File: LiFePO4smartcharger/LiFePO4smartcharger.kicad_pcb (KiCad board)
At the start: 2 copper layers, 99.3 x 98.6 mm, 106 parts, among them J1 Conn_01x02, J10 Conn_01x01, J11 Conn_01x01, J12 Conn_01x04, J13 Conn_01x01, J14 Conn_01x02, J2 Conn_02x03_Odd_Even, J3 Conn_01x02, J4 Conn_01x02, J5 Conn_01x02, J6 Conn_01x01, J7 Conn_01x01, J8 Conn_01x02, J9 Conn_01x02, Q1 TIP42, Q2 TIP41, Q3 2N3906, Q4 TIP41C, T1 Transformer_1P1Sdotted, U1 ATMEGA328P-PU, U2 LM358, U3 LCD-016N002L, U4 TL494, U9 LM7805_TO220, X3 16MHz

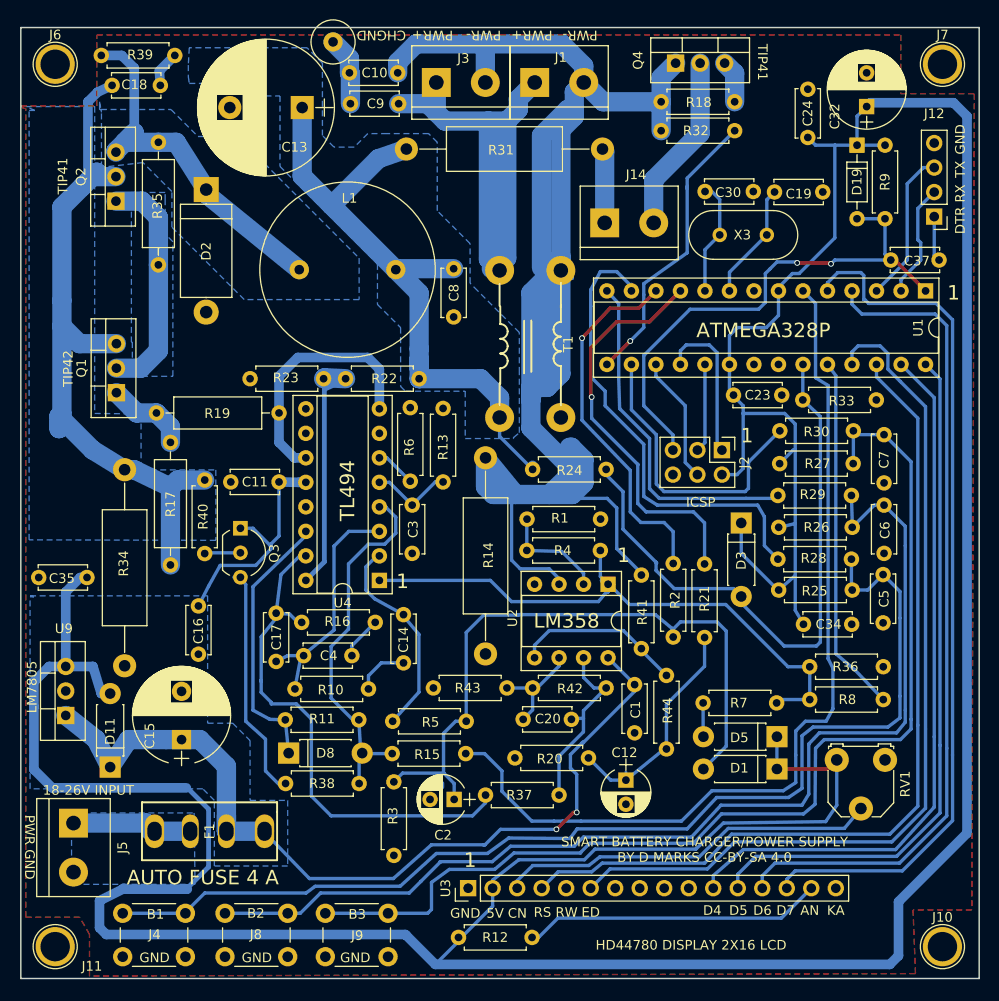
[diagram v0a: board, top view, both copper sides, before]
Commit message: Fixes to allow for larger components
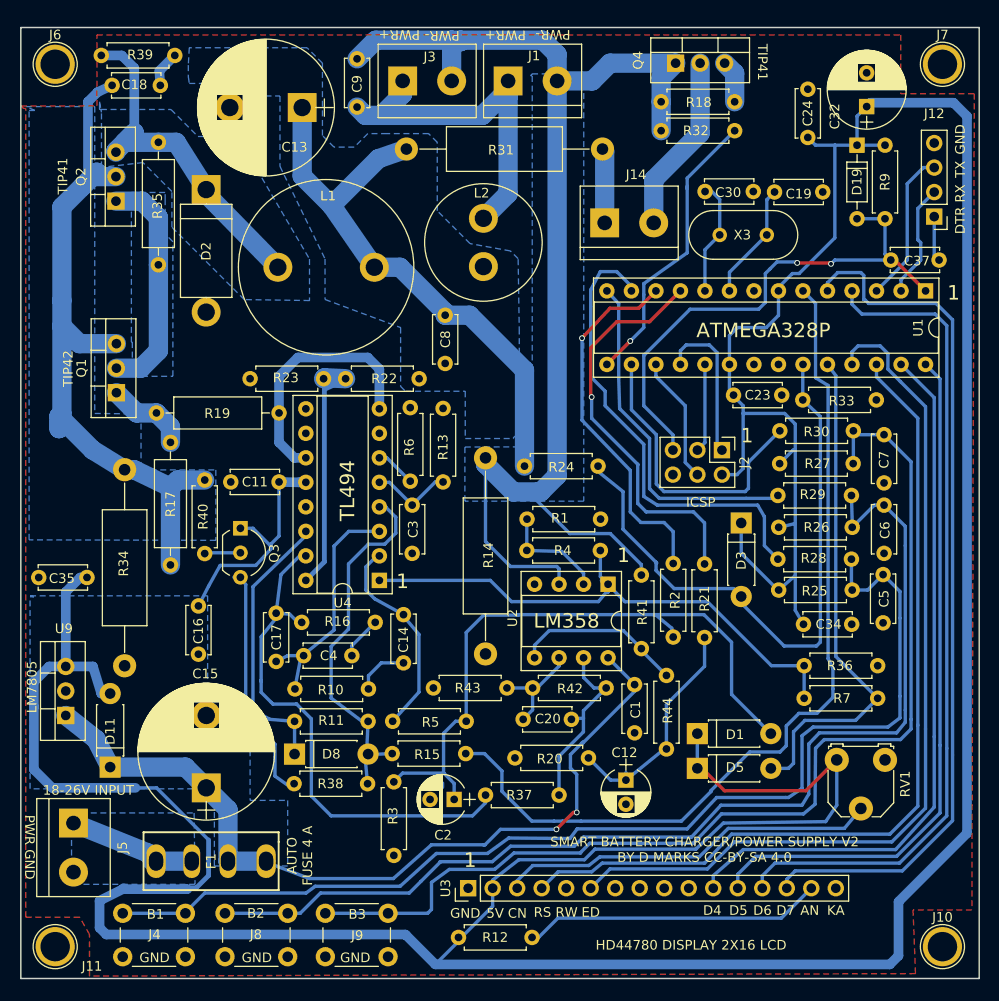
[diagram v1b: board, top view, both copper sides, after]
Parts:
- removed C10: 100nF, Capacitors_THT:C_Disc_D5.0mm_W2.5mm_P5.00mm
- removed J13: Conn_01x01, Connectors:1pin
- removed R8: 10k, Resistors_THT:R_Axial_DIN0207_L6.3mm_D2.5mm_P7.62mm_Horizontal
- removed T1: Transformer_1P1Sdotted, LiFePO4smartcharger:GenericCMCL3
- added L2: 10 uH, Inductors_THT:L_Radial_D12.0mm_P5.00mm_Fastron_11P, F.Cu at (90.2, 55.0)
- C15: footprint Capacitors_THT:CP_Radial_D10.0mm_P5.00mm -> Capacitors_THT:CP_Radial_D14.0mm_P7.50mm
- moved R7 18.1 mm to (131.0, 99.7), turned to 180 degrees
- moved D1 9.03 mm to (112.3, 103.4), turned to 0 degrees
- moved D5 8.88 mm to (112.3, 107.0), turned to 0 degrees
- moved C15 5.62 mm to (61.5, 109.0)
- moved C8 4.90 mm to (86.2, 60.0)
- moved C9 4.32 mm to (77.1, 38.5), turned to 90 degrees
- moved J3 3.49 mm to (81.8, 35.7)
- moved F1 3.10 mm to (62.0, 116.6)
- moved J1 2.76 mm to (92.7, 35.7)
- moved L1 2.23 mm to (68.9, 55.0)
- moved R11 0.97 mm to (70.6, 102.1)
- moved R24 0.91 mm to (102.1, 75.7)
- moved R38 0.88 mm to (78.2, 108.6)
- moved D8 0.62 mm to (70.6, 105.5)
- moved R36 0.59 mm to (123.4, 96.3)
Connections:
- C9 pad 2: Net-(C10-Pad1) -> CURRENTSHUNT
- D5 pad 2: Net-(D5-Pad2) -> A1
- R7 pad 1: Net-(D5-Pad2) -> A1
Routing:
- net CURRENTSHUNT: track 191.0 -> 139.8 mm
- net A1: track 38.0 -> 53.5 mm
- net Net-(C9-Pad1): track 52.9 -> 37.6 mm
- net Net-(C13-Pad1): track 69.5 -> 59.9 mm
- net +5V: track 421.4 -> 430.8 mm
- net Net-(C10-Pad1): track 7.15 -> 0.00 mm
- net +24V: track 117.4 -> 111.8 mm
- net Net-(R36-Pad1): track 65.7 -> 61.0 mm
- net Net-(D5-Pad2): track 3.51 -> 0.00 mm
- net SHUTDOWN: track 95.0 -> 92.3 mm
- net Net-(C2-Pad1): track 70.8 -> 68.9 mm
- net Net-(D2-Pad1): track 40.9 -> 39.1 mm
- net Net-(D8-Pad1): track 27.9 -> 28.8 mm
- net A0: track 63.6 -> 64.5 mm
- net Net-(F1-Pad2): track 12.5 -> 13.2 mm
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- added copper zone on B.Cu, net CURRENTSHUNT
- removed copper zone on B.Cu, net Net-(C9-Pad1)
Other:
- board text added: "SMART BATTERY CHARGER/POWER SUPPLY V2 BY D MARKS CC-BY-SA 4.0"
- board text removed: "CHGND"
- board text removed: "SMART BATTERY CHARGER/POWER SUPPLY BY D MARKS CC-BY-SA 4.0"

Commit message: Before switching VOLTAGESET CURRENTSET pins
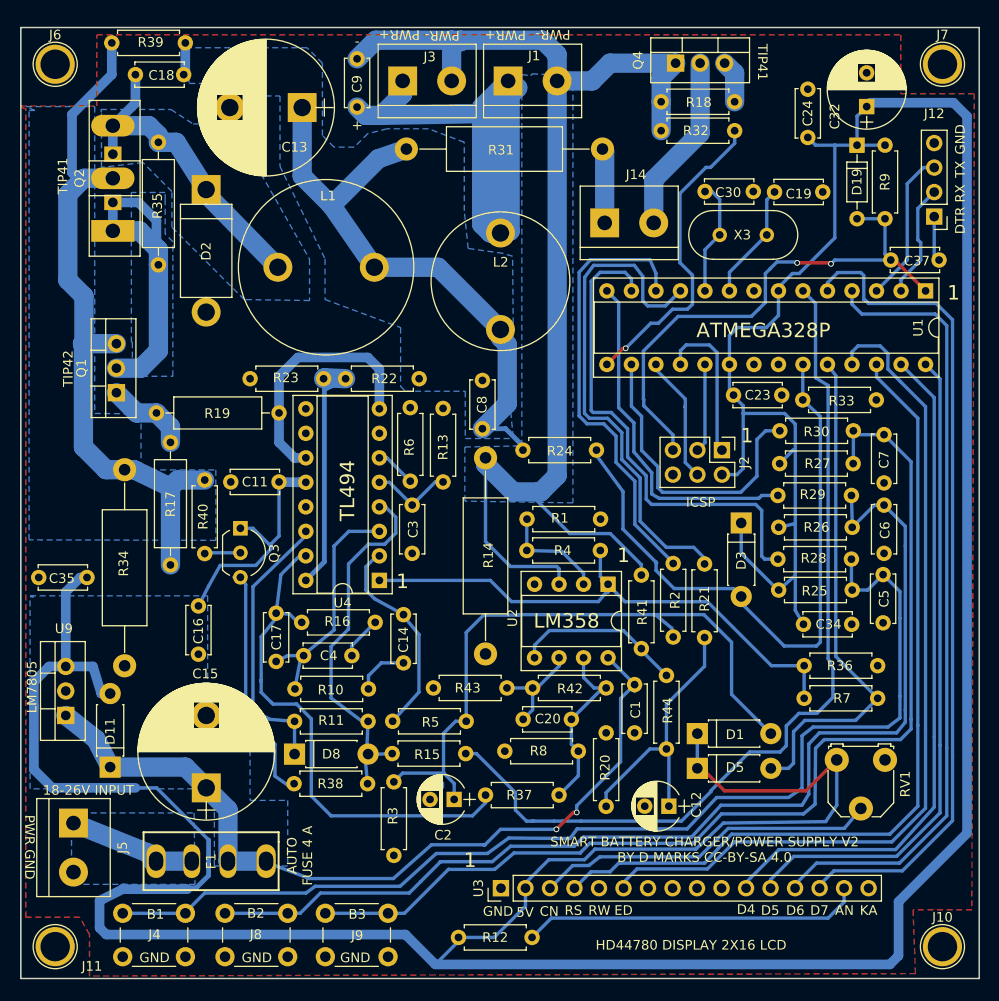
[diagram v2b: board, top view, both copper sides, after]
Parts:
- added R8: 10k, Resistors_THT:R_Axial_DIN0207_L6.3mm_D2.5mm_P7.62mm_Horizontal, F.Cu at (92.4, 105.2)
- C13: value 100 uF -> 1000 uF
- C15: value 10 uF -> 1000 uF
- C8: value 100nF -> 10 uF
- L2: footprint Inductors_THT:L_Radial_D12.0mm_P5.00mm_Fastron_11P -> Inductors_THT:L_Radial_D14.2mm_P10.00mm_Neosid_SD14
- Q2: footprint TO_SOT_Packages_THT:TO-220-3_Vertical -> LiFePO4smartcharger:TO-247_TO-3P_Vertical
- moved C8 12.4 mm to (90.1, 71.8), turned to 90 degrees
- moved R20 9.80 mm to (102.9, 103.3), turned to 270 degrees
- moved L2 6.76 mm to (92.0, 61.5)
- moved C12 5.21 mm to (109.4, 110.9), turned to 180 degrees
- moved U3 3.40 mm to (92.0, 119.4)
- moved Q2 3.10 mm to (51.8, 51.3)
- moved C18 2.81 mm to (54.1, 35.1), turned to 0 degrees
- moved R39 1.70 mm to (59.3, 31.8)
- moved R24 1.67 mm to (101.9, 74.0)
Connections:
- D2 pad 1: Net-(D2-Pad1) -> Net-(C18-Pad1)
- L1 pad 1: Net-(D2-Pad1) -> Net-(C18-Pad1)
- Q1 pad 3: Net-(C18-Pad2) -> Net-(Q1-Pad3)
- Q2 pad 2: Net-(C18-Pad2) -> Net-(Q1-Pad3)
- Q2 pad 3: Net-(D2-Pad1) -> Net-(C18-Pad1)
- R17 pad 2: Net-(C18-Pad2) -> Net-(Q1-Pad3)
- R34 pad 2: Net-(C18-Pad2) -> Net-(Q1-Pad3)
- R35 pad 2: Net-(D2-Pad1) -> Net-(C18-Pad1)
- R39 pad 1: Net-(C18-Pad1) -> Net-(C18-Pad2)
- R39 pad 2: Net-(D2-Pad1) -> Net-(Q1-Pad3)
- R40 pad 1: Net-(C18-Pad2) -> Net-(Q1-Pad3)
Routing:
- net Net-(Q1-Pad3): track 0.00 -> 77.8 mm
- net Net-(C18-Pad2): track 76.9 -> 3.36 mm
- net Net-(D2-Pad1): track 39.1 -> 0.00 mm
- net Net-(C9-Pad1): track 37.6 -> 73.4 mm
- net Net-(C18-Pad1): track 3.77 -> 33.8 mm
- net VOLTAGESET: track 42.2 -> 52.8 mm, vias 1 -> 0
- net Net-(Q1-Pad2): track 24.0 -> 34.0 mm
- net CURRENTSET: track 38.4 -> 46.6 mm, vias 1 -> 0
- net Net-(C12-Pad1): track 24.5 -> 29.3 mm
- net Net-(R12-Pad2): track 31.1 -> 35.3 mm
- net DB6: track 85.9 -> 82.0 mm
- net Net-(RV1-Pad2): track 39.5 -> 35.7 mm
- net DB7: track 91.5 -> 87.8 mm
- net DB5: track 72.1 -> 68.4 mm
- net DB4: track 74.5 -> 70.8 mm
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- added copper zone on B.Cu, net Net-(C18-Pad1)
- added copper zone on B.Cu, net Net-(Q1-Pad3)
- removed copper zone on B.Cu, net Net-(C18-Pad2)
- removed copper zone on B.Cu, net Net-(D2-Pad1)
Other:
- board text added: "+"
- board text added: "-"

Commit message: JLCPCB order 2021-04-11
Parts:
- moved R18 7.68 mm to (116.3, 37.6), turned to 180 degrees
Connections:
- Q4 pad 1: CURRENTSHUNT -> Net-(Q4-Pad1)
- Q4 pad 3: Net-(Q4-Pad3) -> CURRENTSHUNT
- R18 pad 2: Net-(Q4-Pad3) -> Net-(Q4-Pad1)
- R32 pad 1: CURRENTSHUNT -> Net-(Q4-Pad1)
- U1 pad 11: VOLTAGESET -> DRAINBASE
- U1 pad 12: CURRENTSET -> BUTTON1
- U1 pad 13: BUTTON1 -> BUTTON2
- U1 pad 14: BUTTON2 -> BUTTON3
- U1 pad 15: DRAINBASE -> CURRENTSET
- U1 pad 16: BUTTON3 -> VOLTAGESET
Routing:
- net VOLTAGESET: track 52.8 -> 24.8 mm
- net CURRENTSET: track 46.6 -> 24.3 mm
- net BUTTON2: track 36.2 -> 50.8 mm, vias 0 -> 2
- net BUTTON3: track 31.6 -> 45.9 mm, vias 0 -> 2
- net DRAINBASE: track 32.7 -> 20.5 mm, vias 1 -> 0
- net BUTTON1: track 52.1 -> 61.4 mm, vias 0 -> 2
- net Net-(Q4-Pad1): track 0.00 -> 7.73 mm
- net CURRENTSHUNT: track 139.8 -> 144.5 mm
- net Net-(Q4-Pad3): track 4.43 -> 0.00 mm

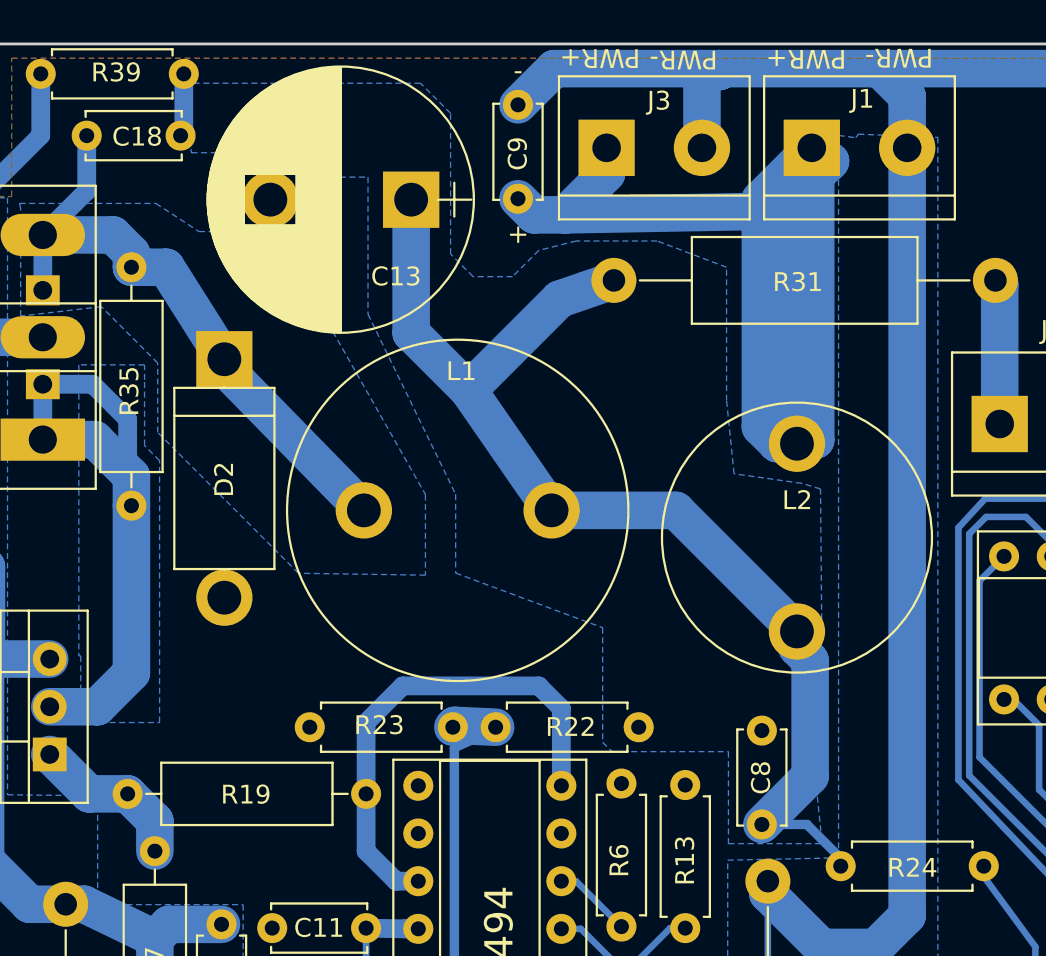
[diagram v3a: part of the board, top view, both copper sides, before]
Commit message: Removed on-board RF filter inductor
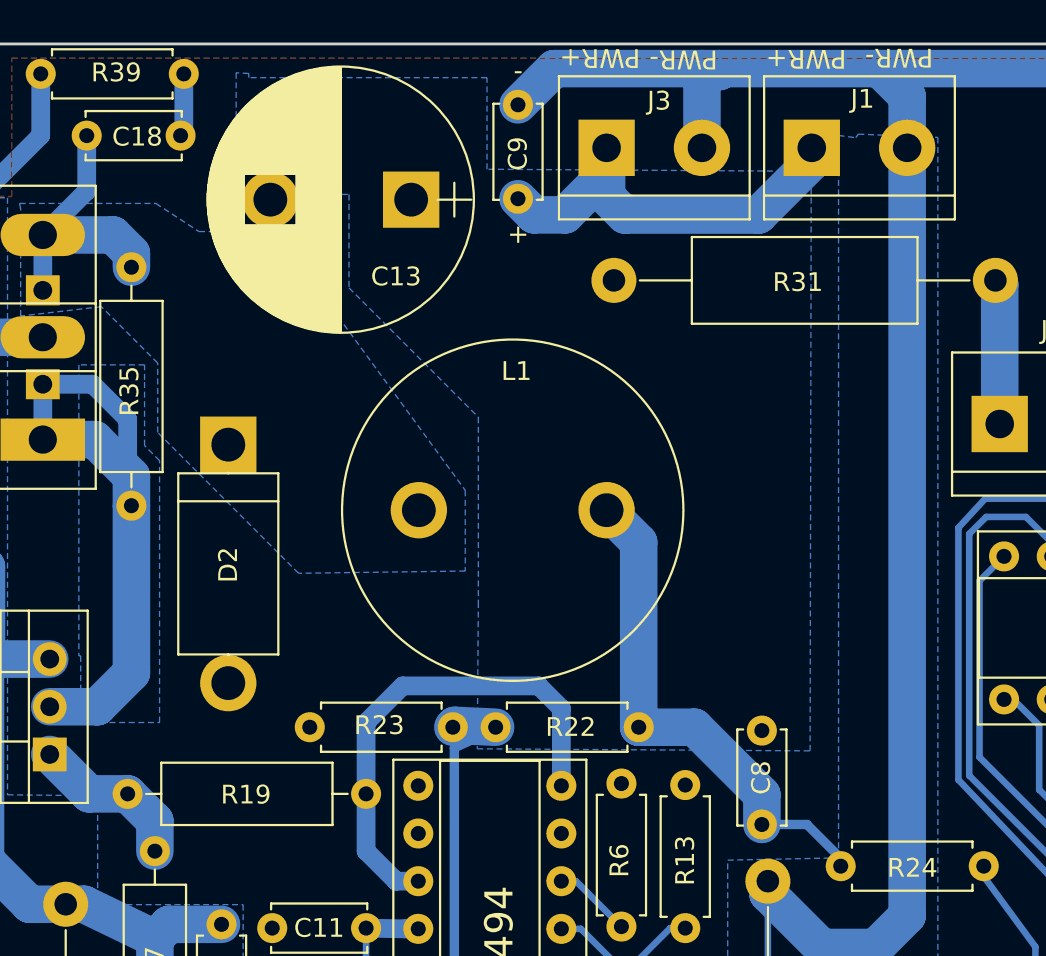
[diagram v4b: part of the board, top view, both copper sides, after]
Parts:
- removed L2: 10 uH, Inductors_THT:L_Radial_D14.2mm_P10.00mm_Neosid_SD14
- moved D2 4.55 mm to (61.7, 51.5)
- moved L1 2.93 mm to (71.8, 55.0)
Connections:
- C9 pad 1: Net-(C9-Pad1) -> Net-(C13-Pad1)
- J1 pad 1: Net-(C9-Pad1) -> Net-(C13-Pad1)
- J3 pad 1: Net-(C9-Pad1) -> Net-(C13-Pad1)
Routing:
- net Net-(C9-Pad1): track 73.4 -> 0.00 mm
- net Net-(C18-Pad1): track 33.8 -> 15.1 mm
- net Net-(C13-Pad1): track 62.3 -> 52.1 mm

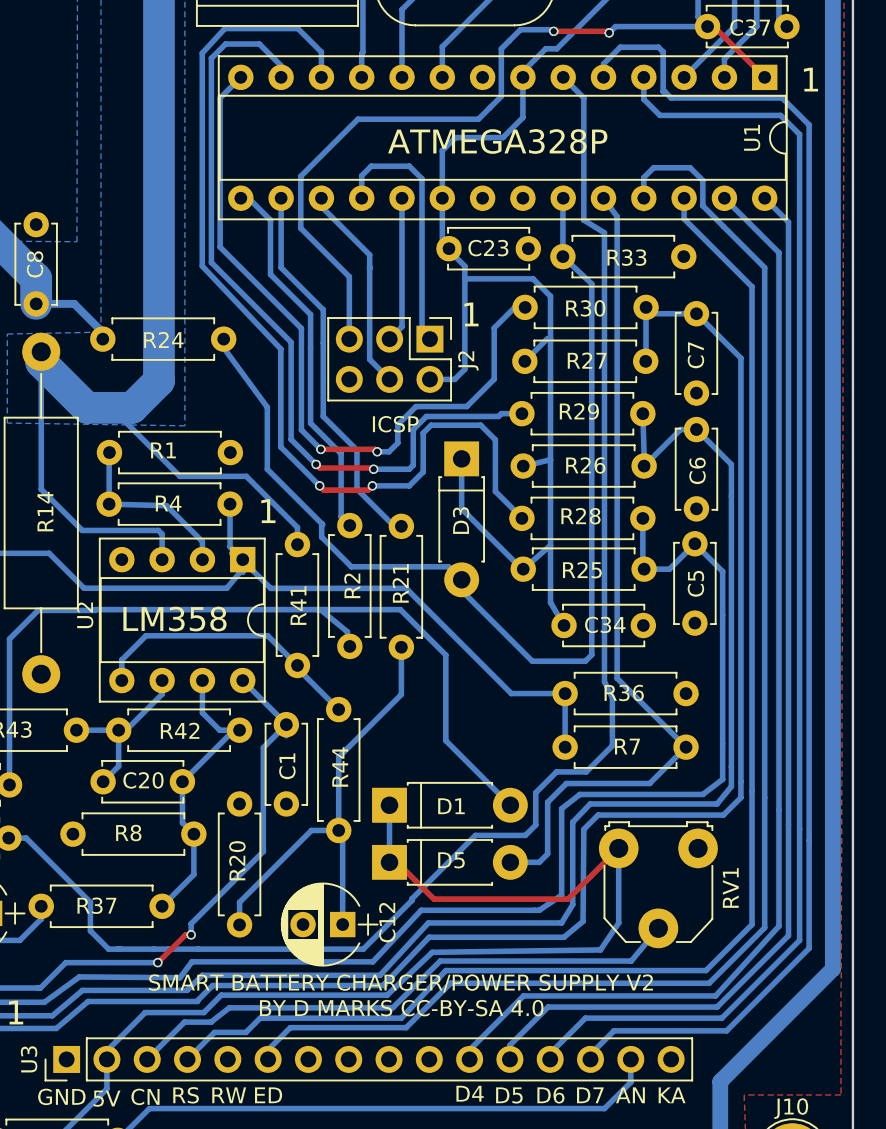
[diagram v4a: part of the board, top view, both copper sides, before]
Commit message: Added spot for LM35 temperature sensor
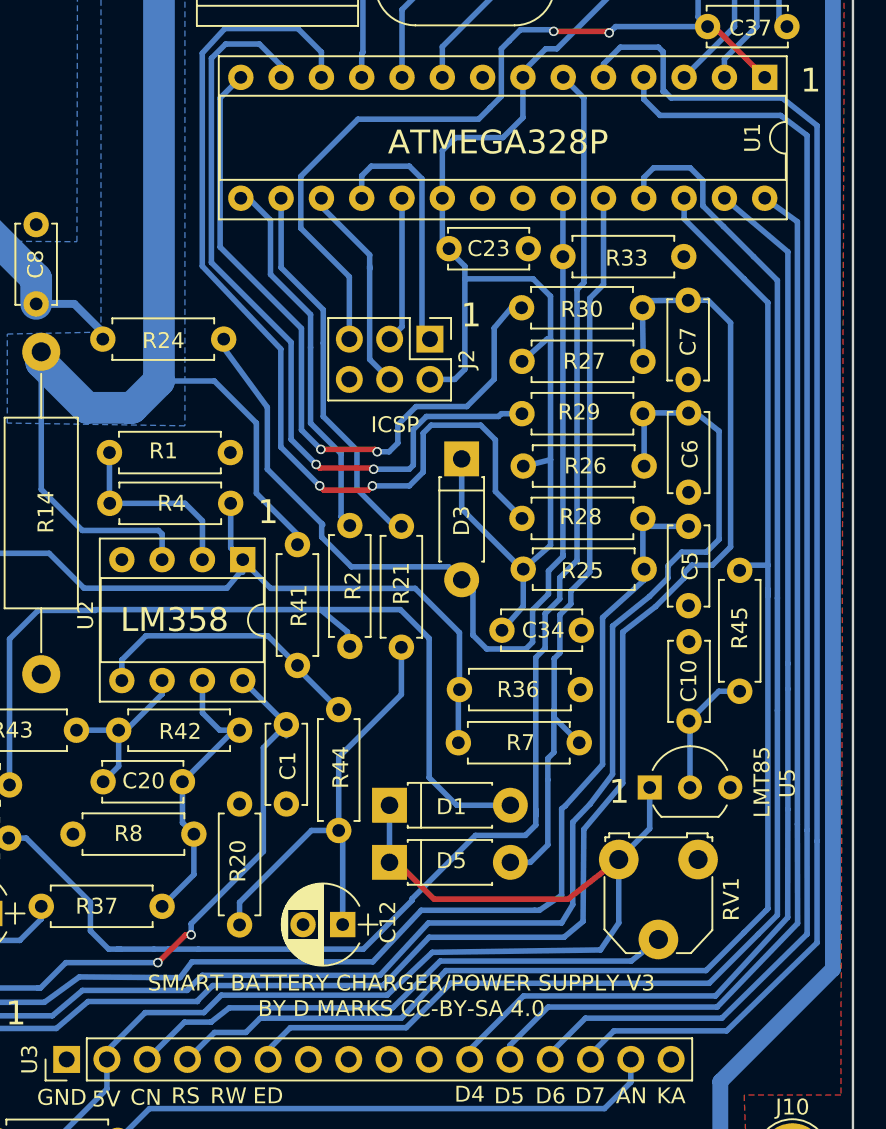
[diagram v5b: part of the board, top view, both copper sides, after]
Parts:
- added C10: 1000 pF, Capacitors_THT:C_Disc_D5.0mm_W2.5mm_P5.00mm, F.Cu at (131.2, 98.1)
- added R45: 10k, Resistors_THT:R_Axial_DIN0207_L6.3mm_D2.5mm_P7.62mm_Horizontal, F.Cu at (134.4, 88.6)
- added U5: LMT85, TO_SOT_Packages_THT:TO-92_Inline_Wide, F.Cu at (128.8, 102.3)
- R1: value 6k8 -> 10k
- R23, R33: value 2k7 -> 2k2
- R41: value 470k -> 620k
- R42: value 2k2 -> 1k8
- moved R4 7.58 mm to (94.7, 84.3), turned to 0 degrees
- moved R7 6.74 mm to (124.3, 99.4)
- moved R36 6.66 mm to (116.8, 96.1)
- moved C34 3.92 mm to (119.4, 92.3)
- moved C5 1.17 mm to (131.2, 85.8)
- moved C6 1.16 mm to (131.2, 78.7)
- moved C7 1.00 mm to (131.2, 71.5)
- moved RV1 0.70 mm to (131.8, 106.8)
- moved R30 0.23 mm to (120.7, 72.0)
- moved R27 0.18 mm to (128.3, 75.4)
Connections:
- J10 pad 1: (no net) -> Net-(J10-Pad1)
- J11 pad 1: (no net) -> Net-(J11-Pad1)
- J6 pad 1: (no net) -> Net-(J6-Pad1)
- J7 pad 1: (no net) -> Net-(J7-Pad1)
- R4 pad 1: Net-(R36-Pad1) -> Net-(R1-Pad1)
- R4 pad 2: Net-(R1-Pad1) -> Net-(R36-Pad1)
- U1 pad 21: (no net) -> Net-(U1-Pad21)
- U3 pad 10: (no net) -> Net-(U3-Pad10)
- U3 pad 7: (no net) -> Net-(U3-Pad7)
- U3 pad 8: (no net) -> Net-(U3-Pad8)
- U3 pad 9: (no net) -> Net-(U3-Pad9)
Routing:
- net Net-(C5-Pad1): track 115.4 -> 105.5 mm
- net Net-(C10-Pad1): track 0.00 -> 8.19 mm
- net Net-(R36-Pad1): track 61.0 -> 56.0 mm
- net A1: track 53.5 -> 48.6 mm
- net Net-(C6-Pad1): track 113.2 -> 109.2 mm
- net +5V: track 431.1 -> 434.8 mm
- net RS: track 86.9 -> 90.0 mm
- net A0: track 65.8 -> 62.9 mm
- net Net-(C7-Pad1): track 111.2 -> 108.9 mm
- net SHUTDOWN: track 92.3 -> 90.3 mm
- net Net-(C2-Pad1): track 68.9 -> 70.9 mm
- net CURRENTSHUNT: track 144.5 -> 143.0 mm
- net Net-(R1-Pad1): track 11.6 -> 12.4 mm
- net EDISP: track 90.1 -> 90.7 mm
- net DB4: track 70.8 -> 71.4 mm
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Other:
- board text added: "LMT85"
- board text added: "SMART BATTERY CHARGER/POWER SUPPLY V3 BY D MARKS CC-BY-SA 4.0"
- board text removed: "SMART BATTERY CHARGER/POWER SUPPLY V2 BY D MARKS CC-BY-SA 4.0"
